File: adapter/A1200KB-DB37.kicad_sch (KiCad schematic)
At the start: 41 parts, among them J1 Molex 52044-3245, J2 LED HDR, J3 DB37 female RA

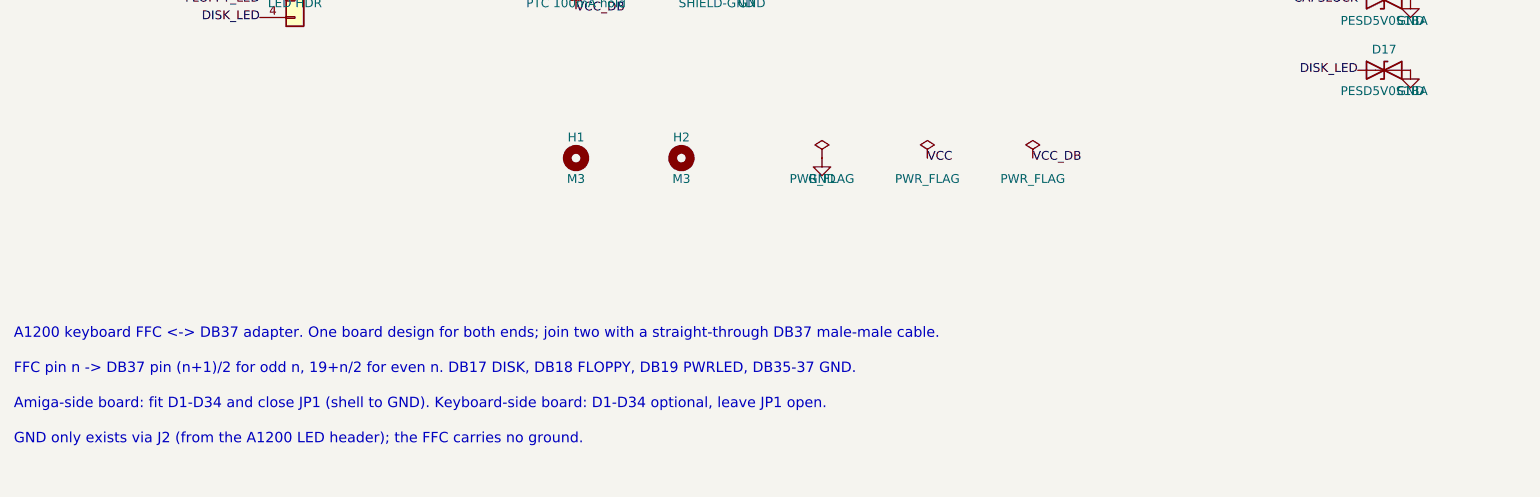
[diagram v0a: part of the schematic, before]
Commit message: add floppy power header for ground, move h1 to make room.
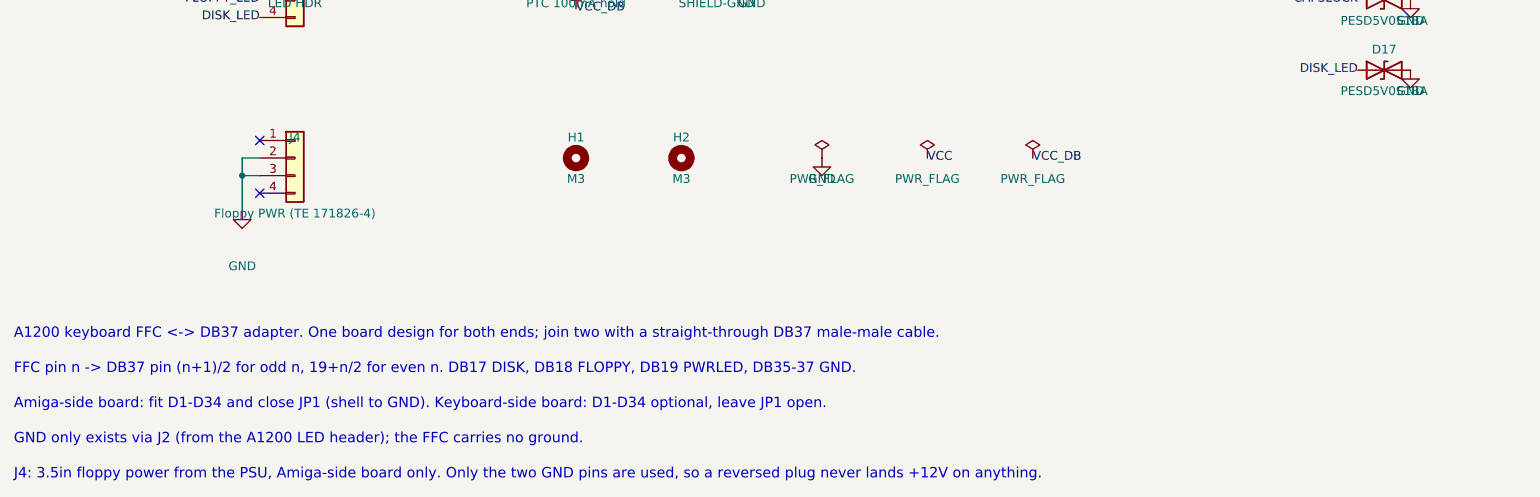
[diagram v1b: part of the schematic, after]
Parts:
- added J4: Floppy PWR (TE 171826-4), Connector_Floppy:TE_171826-4_1x04_P2.50mm_Horizontal, symbol Connector_Generic:Conn_01x04
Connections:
- net GND: now also J4.2 (Pin_2), J4.3 (Pin_3)
- no-connect marks 1 -> 3
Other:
- note added: "J4: 3.5in floppy power from the PSU, Amiga-side board only. Only the two GND pins are used, so a reversed plug never lands +12V on anything."

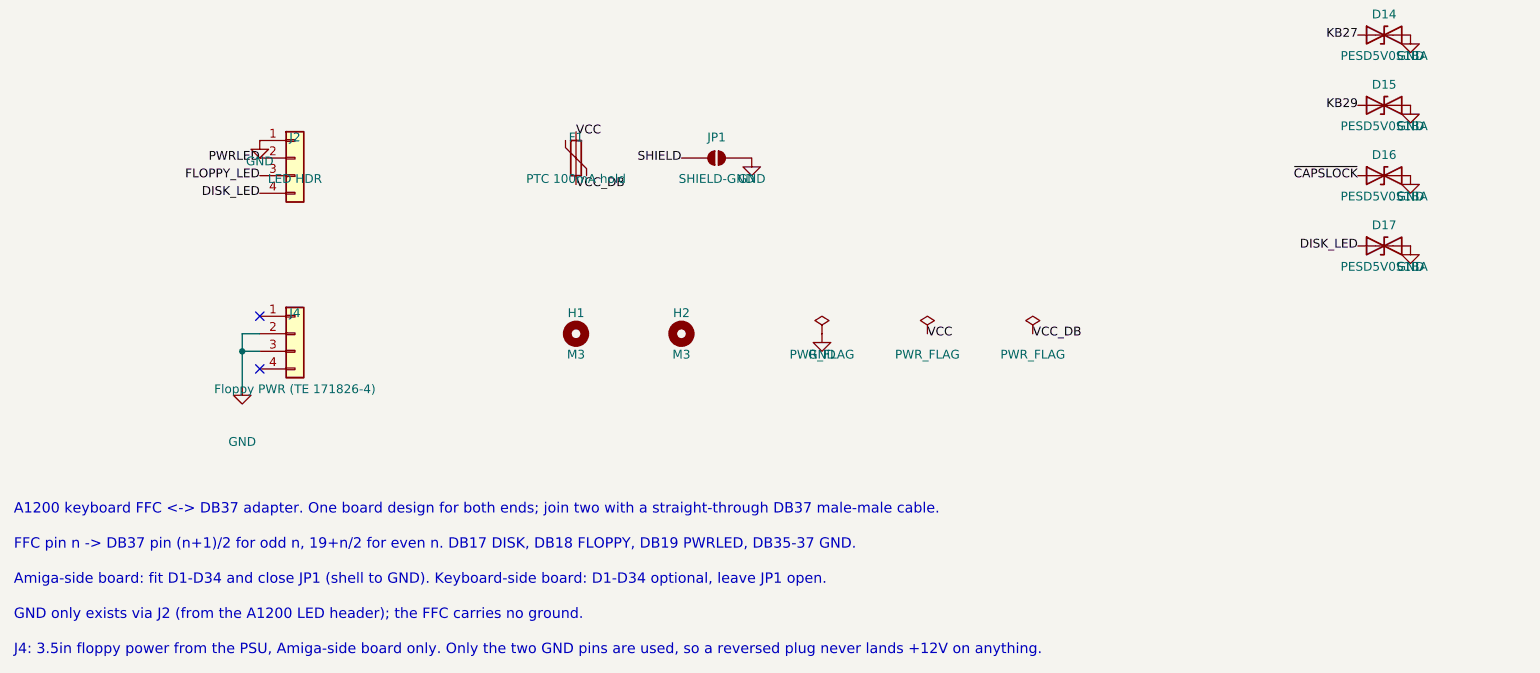
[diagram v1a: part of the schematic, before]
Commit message: replace floppy header with symmetric 5-pin led header for safe reversal.
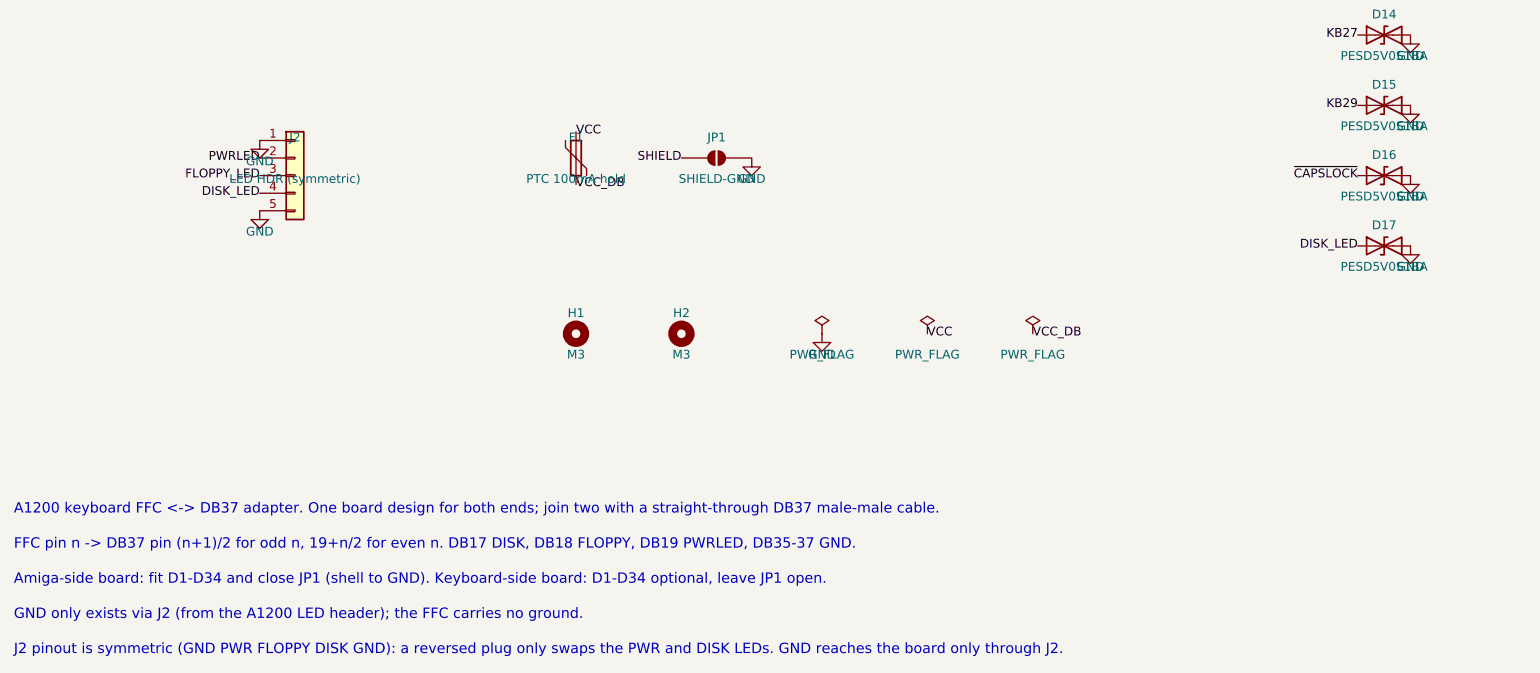
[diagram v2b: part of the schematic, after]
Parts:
- removed J4: Floppy PWR (TE 171826-4), Connector_Floppy:TE_171826-4_1x04_P2.50mm_Horizontal, symbol Connector_Generic:Conn_01x04
- J2: value LED HDR -> LED HDR (symmetric); footprint Connector_PinHeader_2.54mm:PinHeader_1x04_P2.54mm_Vertical -> Connector_PinHeader_2.54mm:PinHeader_1x05_P2.54mm_Horizontal; symbol Connector_Generic:Conn_01x04 -> Connector_Generic:Conn_01x05
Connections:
- net GND: now also J2.5 (Pin_5)
- no-connect marks 3 -> 1
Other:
- note added: "J2 pinout is symmetric (GND PWR FLOPPY DISK GND): a reversed plug only swaps the PWR and DISK LEDs. GND reaches the board only through J2."
- note removed: "J4: 3.5in floppy power from the PSU, Amiga-side board only. Only the two GND pins are used, so a reversed plug never lands +12V on anything."
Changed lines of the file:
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@@
 	)
 	(symbol
-		(lib_id "Connector_Generic:Conn_01x04")
-		(at 60.96 190.5 0)
+		(lib_id "Connector_Generic:Conn_01x05")
+		(at 60.96 193.04 0)
 		(unit 1)
 		(body_style 1)
@@
 			)
 		)
-		(property "Value" "LED HDR"
+		(property "Value" "LED HDR (symmetric)"
 			(at 60.96 193.5 0)
 			(show_name no)
@@
 			)
 		)
-		(property "Footprint" "Connector_PinHeader_2.54mm:PinHeader_1x04_P2.54mm_Vertical"
+		(property "Footprint" "Connector_PinHeader_2.54mm:PinHeader_1x05_P2.54mm_Horizontal"
 			(at 60.96 190.5 0)
 			(hide yes)
@@
 		(pin "4"
 		)
+		(pin "5")
 		(instances
 			(project "A1200KB-DB37"
@@
 		)
 	)
-	(symbol (lib_id "Connector_Generic:Conn_01x04") (at 60.96 215.9 0) (unit 1) (exclude_from_sim no) (in_bom yes) (on_board yes) (dnp no) (property "Reference" "J4" (at 60.96 212.9 0) (effects (font (size 1.27 1.27)))) (property "Value" "Floppy PWR (TE 171826-4)" (at 60.96 223.9 0) (effects (font (size 1.27 1.27)))) (property "Footprint" "Connector_Floppy:TE_171826-4_1x04_P2.50mm_Horizontal" (at 60.96 215.9 0) (effects (font (size 1.27 1.27)) (hide yes))) (property "Datasheet" "" (at 60.96 215.9 0) (effects (font (size 1.27 1.27)) (hide yes))) (pin "1")(pin "2")(pin "3")(pin "4") (instances (project "A1200KB-DB37" (path "/45c9f657-c017-55d4-9343-478dd02f86d1" (reference "J4") (unit 1)))))
-	(no_connect (at 55.88 213.36))
-	(no_connect (at 55.88 220.98))
-	(wire (pts (xy 55.88 215.9) (xy 53.34 215.9)) (stroke (width 0) (type default)))
-	(wire (pts (xy 55.88 218.44) (xy 53.34 218.44)) (stroke (width 0) (type default)))
-	(wire (pts (xy 53.34 215.9) (xy 53.34 223.52)) (stroke (width 0) (type default)))
-	(junction (at 53.34 218.44) (diameter 0) (color 0 0 0 0))
-	(symbol (lib_id "power:GND") (at 53.34 223.52 0) (unit 1) (exclude_from_sim no) (in_bom yes) (on_board yes) (dnp no) (property "Reference" "#PWR41" (at 53.34 220.52 0) (effects (font (size 1.27 1.27)) (hide yes))) (property "Value" "GND" (at 53.34 231.52 0) (effects (font (size 1.27 1.27)))) (property "Footprint" "" (at 53.34 223.52 0) (effects (font (size 1.27 1.27)) (hide yes))) (property "Datasheet" "" (at 53.34 223.52 0) (effects (font (size 1.27 1.27)) (hide yes))) (pin "1") (instances (project "A1200KB-DB37" (path "/45c9f657-c017-55d4-9343-478dd02f86d1" (reference "#PWR41") (unit 1)))))
-	(text "J4: 3.5in floppy power from the PSU, Amiga-side board only. Only the two GND pins are used, so a reversed plug never lands +12V on anything." (exclude_from_sim no) (at 20.32 261.62 0) (effects (font (size 1.5 1.5)) (justify left)))
+	(symbol (lib_id "power:GND") (at 55.88 198.12 0) (unit 1) (exclude_from_sim no) (in_bom yes) (on_board yes) (dnp no) (property "Reference" "#PWR42" (at 55.88 195.12 0) (effects (font (size 1.27 1.27)) (hide yes))) (property "Value" "GND" (at 55.88 201.12 0) (effects (font (size 1.27 1.27)))) (property "Footprint" "" (at 55.88 198.12 0) (effects (font (size 1.27 1.27)) (hide yes))) (property "Datasheet" "" (at 55.88 198.12 0) (effects (font (size 1.27 1.27)) (hide yes))) (pin "1") (instances (project "A1200KB-DB37" (path "/45c9f657-c017-55d4-9343-478dd02f86d1" (reference "#PWR42") (unit 1)))))
+	(text "J2 pinout is symmetric (GND PWR FLOPPY DISK GND): a reversed plug only swaps the PWR and DISK LEDs. GND reaches the board only through J2." (exclude_from_sim no) (at 20.32 261.62 0) (effects (font (size 1.5 1.5)) (justify left)))
 	(sheet_instances
 		(path "/"

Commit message: refit db37 edge offset to suit the sockets lcsc actually stocks.
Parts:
- J3: footprint Connector_Dsub:DSUB-37_Socket_Horizontal_P2.77x2.84mm_EdgePinOffset9.90mm_Housed_MountingHolesOffset11.32mm -> Connector_Dsub:DSUB-37_Socket_Horizontal_P2.77x2.84mm_EdgePinOffset7.70mm_Housed_MountingHolesOffset9.12mm
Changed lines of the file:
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@@
 			)
 		)
-		(property "Footprint" "Connector_Dsub:DSUB-37_Socket_Horizontal_P2.77x2.84mm_EdgePinOffset9.90mm_Housed_MountingHolesOffset11.32mm"
+		(property "Footprint" "Connector_Dsub:DSUB-37_Socket_Horizontal_P2.77x2.84mm_EdgePinOffset7.70mm_Housed_MountingHolesOffset9.12mm"
 			(at 152.4 111.76 0)
 			(hide yes)

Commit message: add lcsc part numbers and jlc bom/cpl export for assembly.
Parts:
- D1, D10, D11, D12, D13, D14, D15, D16, D17, D18, D19, D2, D20, D21, D22, D23, D24, D25, D26, D27, D28, D29, D3, D30, D31, D32, D33, D34, D4, D5, D6, D7, D8, D9: LCSC (none) -> C19224; MPN (none) -> PESD5V0S1BA,115
- F1: LCSC (none) -> C70065; MPN (none) -> nSMD010
- J1: MPN (none) -> 52044-3245
- J2: LCSC (none) -> C32713264; MPN (none) -> HX PZ2.54-1x5P WZ
- J3: LCSC (none) -> C77839; MPN (none) -> DS1037-37FNAKT74-0CC
